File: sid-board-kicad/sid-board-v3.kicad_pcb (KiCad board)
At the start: 2 copper layers, 35.4 x 89.2 mm, 49 parts, among them J1 SPI + UART, J2 USB_B_Micro, J3 UART, Q1 BSS138, Q2 BSS138, SW1 SW_EN, SW2 SW_FLASH, U1 SC16IS752IPW, U2 MCP1703A-3302_SOT223, U3 SN65HVD232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

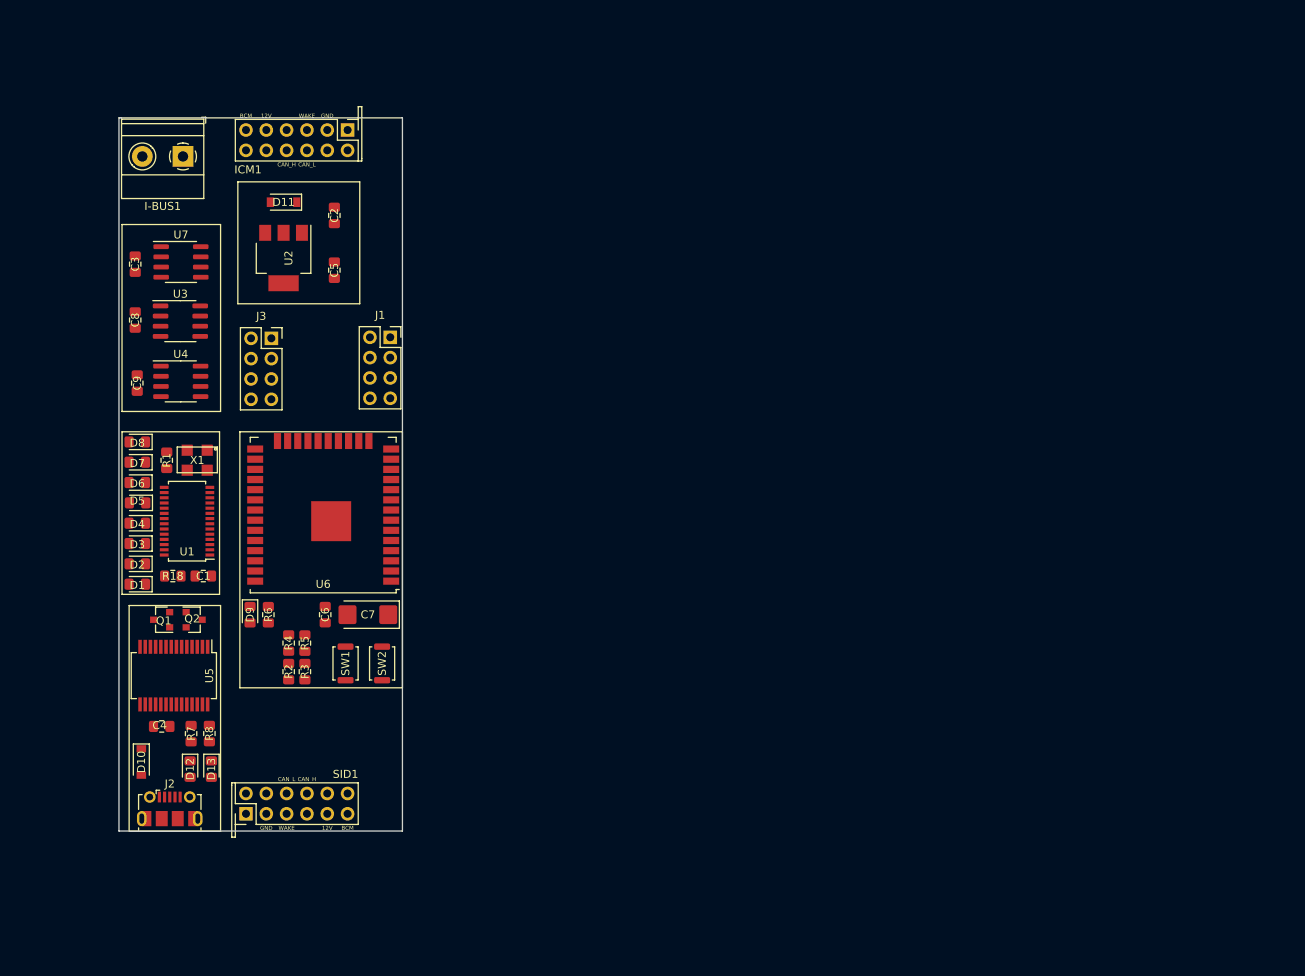
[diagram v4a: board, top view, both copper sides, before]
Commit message: Labelling and reorganisation
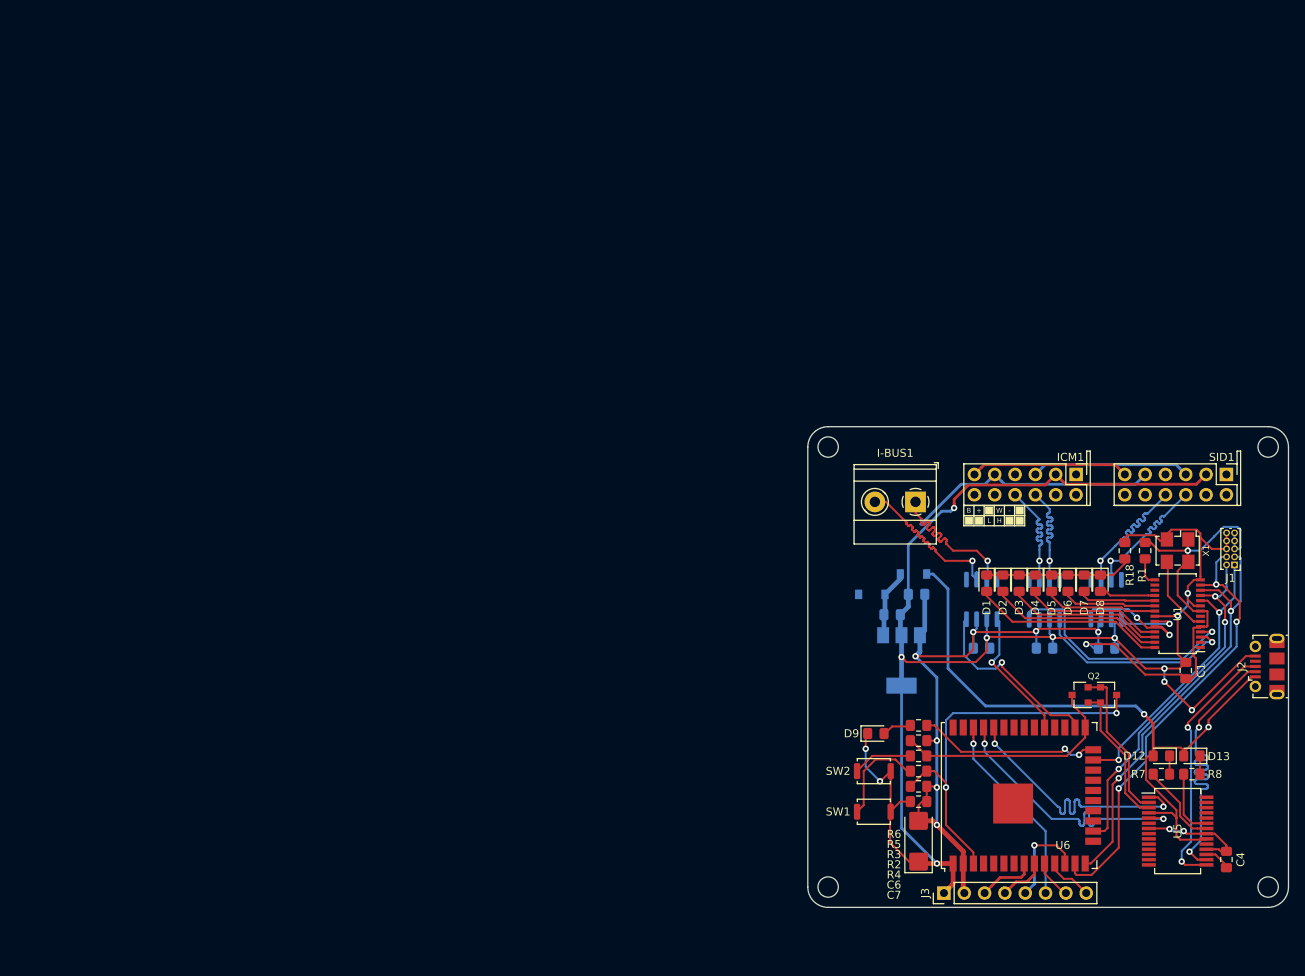
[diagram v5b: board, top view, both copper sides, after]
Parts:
- added ?: , , F.Cu at (123.2, 81.3)
- added ?: , , F.Cu at (121.9, 81.9)
- C2, C3, C5, C8, C9, D10, D11, U2, U3, U4, U7: moved to B.Cu
- J1: footprint Connector_PinSocket_2.54mm:PinSocket_2x04_P2.54mm_Vertical -> Connector_PinHeader_1.00mm:PinHeader_2x05_P1.00mm_Vertical
- J3: value UART -> Conn_01x08; footprint Connector_PinSocket_2.54mm:PinSocket_2x04_P2.54mm_Vertical -> Connector_PinHeader_2.54mm:PinHeader_1x08_P2.54mm_Vertical
- X1: value S53305-24.000-X -> ASE-xxxMHz; footprint sid-board:S53305-16.000-X -> Oscillator:Oscillator_SMD_EuroQuartz_XO53-4Pin_5.0x3.2mm_HandSoldering
- moved J2 138.3 mm to (170.2, 93.2), turned to 90 degrees
- moved C4 134.1 mm to (165.1, 117.3), turned to 90 degrees
- moved U5 127.0 mm to (159.0, 113.8), turned to 0 degrees
- moved C9 125.6 mm to (150.1, 90.9), turned to 0 degrees
- moved U1 124.4 mm to (159.0, 86.6)
- moved C1 123.4 mm to (160.0, 93.7), turned to 90 degrees
- moved X1 123.1 mm to (159.0, 78.7)
- moved R8 122.9 mm to (160.8, 106.7), turned to 0 degrees
- moved R1 122.8 mm to (154.9, 78.7)
- moved D13 122.6 mm to (160.8, 104.4), turned to 180 degrees
- moved D8 121.7 mm to (149.4, 82.8), turned to 270 degrees
- moved D12 121.4 mm to (157.0, 104.4), turned to 180 degrees
- moved R7 121.4 mm to (157.0, 106.7), turned to 0 degrees
- moved C8 120.8 mm to (142.4, 90.9), turned to 0 degrees
- moved D7 119.3 mm to (147.3, 82.8), turned to 270 degrees
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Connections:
- C2 pad 2: Net-(C2-Pad2) -> GND
- C5 pad 2: Net-(C2-Pad2) -> GND
- I-BUS1 pad 1: CAN_L -> CAN_H
- I-BUS1 pad 2: CAN_H -> CAN_L
- ICM1 pad 1: (no net) -> Net-(ICM1-Pad1)
- ICM1 pad 10: CAN_A_L -> CAN_A_H
- ICM1 pad 11: (no net) -> Net-(ICM1-Pad11)
- ICM1 pad 12: (no net) -> Net-(ICM1-Pad12)
- ICM1 pad 4: (no net) -> Net-(ICM1-Pad4)
- ICM1 pad 7: (no net) -> Net-(ICM1-Pad7)
- ICM1 pad 8: (no net) -> Net-(ICM1-Pad8)
- ICM1 pad 9: CAN_A_H -> CAN_A_L
- J1 pad 2: CLK -> MOSI
- J1 pad 3: MOSI -> MISO
- J1 pad 4: MISO -> CLK
- J1 pad 5: GND -> VDD_3.3V
- J1 pad 6: VDD_3.3V -> GND
- J1 pad 7: TXA -> VDD_3.3V
- J1 pad 8: RXA -> GND
- J2 pad 4: (no net) -> Net-(J2-Pad4)
- J3 pad 1: TX_ESP32 -> GND
- J3 pad 2: RX_ESP32 -> VDD_3.3V
- J3 pad 3: TX_ESP32_CAN -> Net-(J3-Pad3)
- J3 pad 4: RX_ESP32_CAN -> Net-(J3-Pad4)
- J3 pad 5: GND -> Net-(J3-Pad5)
- J3 pad 6: VDD_3.3V -> I2S_DIN
- J3 pad 7: TXB -> I2S_WSEL
- J3 pad 8: RXB -> I2S_BCLK
- SID1 pad 1: (no net) -> Net-(SID1-Pad1)
- SID1 pad 10: CAN_B_L -> CAN_B_H
- SID1 pad 11: (no net) -> Net-(SID1-Pad11)
- SID1 pad 12: (no net) -> Net-(SID1-Pad12)
- SID1 pad 4: (no net) -> Net-(SID1-Pad4)
- SID1 pad 7: (no net) -> Net-(SID1-Pad7)
- SID1 pad 8: (no net) -> Net-(SID1-Pad8)
- SID1 pad 9: CAN_B_H -> CAN_B_L
- U1 pad 1: (no net) -> Net-(U1-Pad1)
- U1 pad 16: (no net) -> Net-(U1-Pad16)
- U1 pad 17: (no net) -> Net-(U1-Pad17)
- U1 pad 2: (no net) -> Net-(U1-Pad2)
- U1 pad 7: (no net) -> Net-(U1-Pad7)
- U2 pad 2: Net-(C2-Pad2) -> GND
- U3 pad 5: (no net) -> Net-(U3-Pad5)
- U3 pad 8: (no net) -> Net-(U3-Pad8)
- U4 pad 5: (no net) -> Net-(U4-Pad5)
- U4 pad 8: (no net) -> Net-(U4-Pad8)
- U5 pad 10: (no net) -> Net-(U5-Pad10)
- U5 pad 11: (no net) -> Net-(U5-Pad11)
- U5 pad 12: SLEEP -> Net-(U5-Pad12)
- U5 pad 13: (no net) -> Net-(U5-Pad13)
- U5 pad 14: (no net) -> Net-(U5-Pad14)
- U5 pad 19: (no net) -> Net-(U5-Pad19)
- U5 pad 24: (no net) -> Net-(U5-Pad24)
- U5 pad 25: (no net) -> Net-(U5-Pad25)
- U5 pad 26: (no net) -> Net-(U5-Pad26)
- U5 pad 27: (no net) -> Net-(U5-Pad27)
- U5 pad 28: (no net) -> Net-(U5-Pad28)
- U5 pad 6: RI -> Net-(U5-Pad6)
- U5 pad 8: (no net) -> Net-(U5-Pad8)
- U5 pad 9: (no net) -> Net-(U5-Pad9)
- U6 pad 10: (no net) -> I2S_WSEL
- U6 pad 11: (no net) -> I2S_BCLK
- U6 pad 12: (no net) -> Net-(J3-Pad5)
- U6 pad 17: (no net) -> Net-(U6-Pad17)
- U6 pad 18: (no net) -> Net-(U6-Pad18)
- U6 pad 19: (no net) -> Net-(U6-Pad19)
- U6 pad 20: (no net) -> Net-(U6-Pad20)
- U6 pad 21: (no net) -> Net-(U6-Pad21)
- U6 pad 22: (no net) -> Net-(U6-Pad22)
- U6 pad 27: RI -> Net-(U6-Pad27)
- U6 pad 28: SLEEP -> Net-(U6-Pad28)
- U6 pad 30: (no net) -> Net-(U6-Pad30)
- U6 pad 31: (no net) -> Net-(U6-Pad31)
- U6 pad 32: (no net) -> Net-(U6-Pad32)
- U6 pad 33: (no net) -> Net-(U6-Pad33)
- U6 pad 36: (no net) -> I2S_DIN
- U6 pad 37: (no net) -> Net-(U6-Pad37)
- U6 pad 4: (no net) -> Net-(U6-Pad4)
- U6 pad 5: (no net) -> Net-(U6-Pad5)
- U6 pad 6: (no net) -> Net-(U6-Pad6)
- U6 pad 7: (no net) -> Net-(U6-Pad7)
- U6 pad 8: (no net) -> Net-(J3-Pad3)
- U6 pad 9: (no net) -> Net-(J3-Pad4)
- U7 pad 5: (no net) -> Net-(U7-Pad5)
- U7 pad 8: (no net) -> Net-(U7-Pad8)
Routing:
- net GND: track 0.00 -> 245.0 mm, vias 0 -> 15
- net VDD_3.3V: track 0.00 -> 151.7 mm, vias 0 -> 9
- net VBUS: track 0.00 -> 84.7 mm, vias 0 -> 2
- net CLK: track 0.00 -> 55.3 mm, vias 0 -> 3
- net MISO: track 0.00 -> 53.0 mm, vias 0 -> 2
- net EN: track 0.00 -> 49.7 mm, vias 0 -> 2
- net MOSI: track 0.00 -> 44.3 mm, vias 0 -> 3
- net USB_DM: track 0.00 -> 39.8 mm, vias 0 -> 2
- net CS: track 0.00 -> 36.5 mm, vias 0 -> 2
- net RX_ESP32: track 0.00 -> 35.4 mm, vias 0 -> 2
- net TX_ESP32: track 0.00 -> 35.0 mm, vias 0 -> 2
- net USB_DP: track 0.00 -> 32.6 mm, vias 0 -> 2
- net Net-(D11-Pad2): track 0.00 -> 31.6 mm
- net RXA: track 0.00 -> 31.1 mm, vias 0 -> 1
- net IO0: track 0.00 -> 29.6 mm
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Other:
- board size 35.4 x 89.2 mm -> 60.1 x 60.1 mm
- rule trace_min: 0.2 -> 0.1

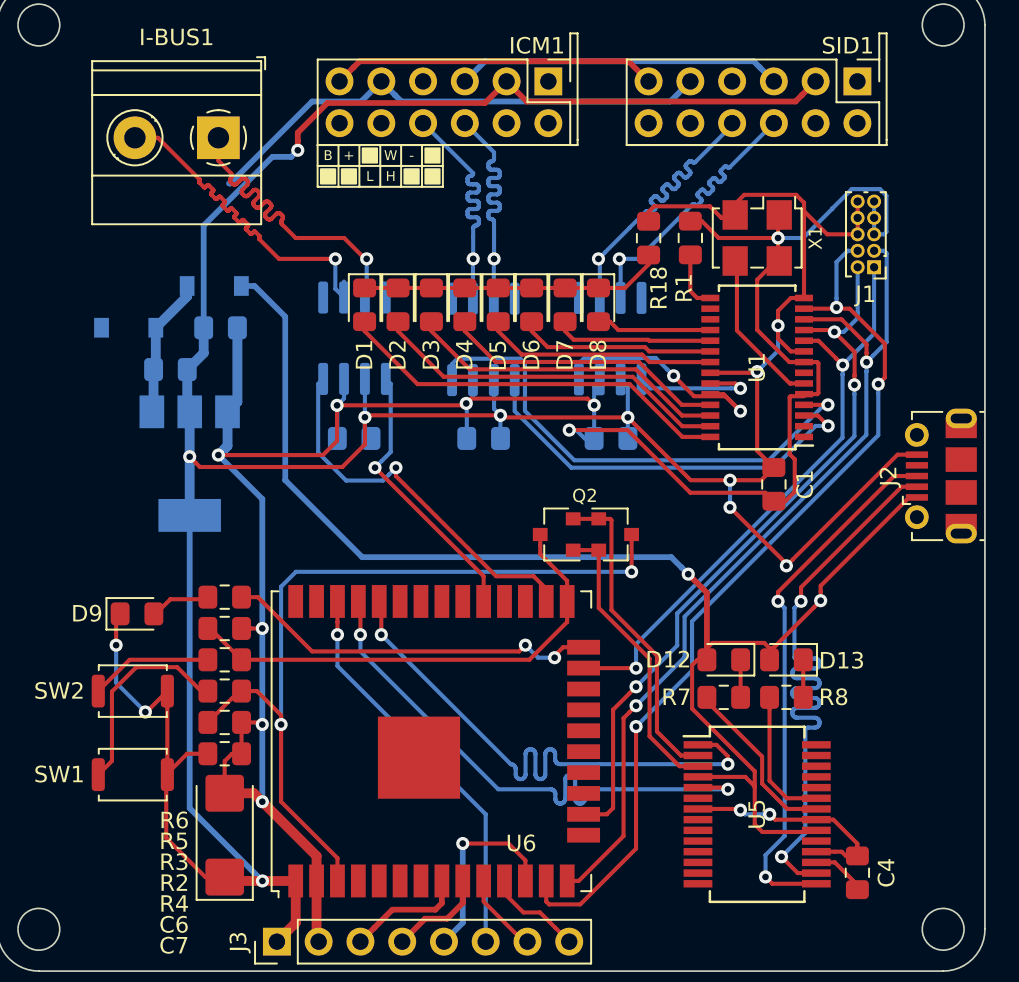
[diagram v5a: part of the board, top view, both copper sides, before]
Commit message: Lost labelling. Moved debug header.
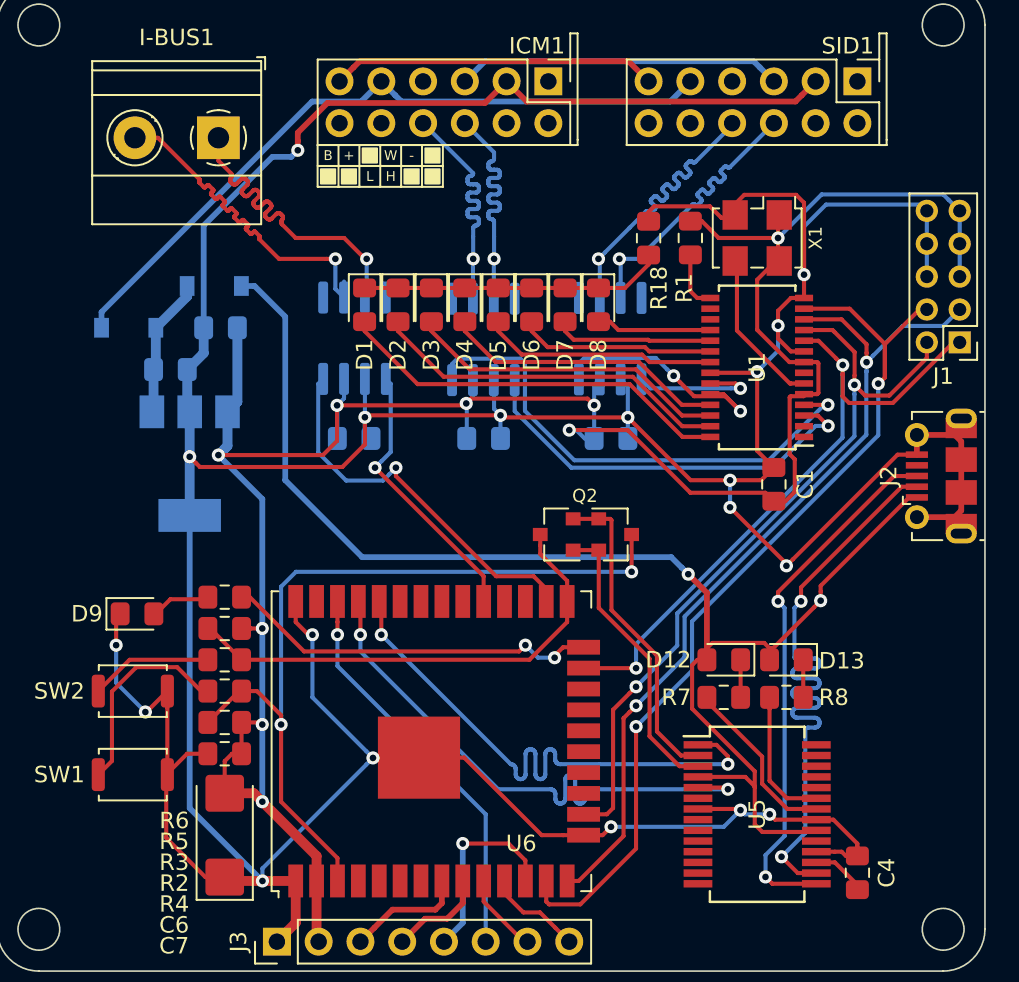
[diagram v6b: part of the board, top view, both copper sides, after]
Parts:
- removed ? (x2): , 
- J1: footprint Connector_PinHeader_1.00mm:PinHeader_2x05_P1.00mm_Vertical -> Connector_PinHeader_2.00mm:PinHeader_2x05_P2.00mm_Vertical
- moved J1 6.93 mm to (171.3, 85.1)
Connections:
- ICM1 pad 1: Net-(ICM1-Pad1) -> (no net)
- ICM1 pad 11: Net-(ICM1-Pad11) -> (no net)
- ICM1 pad 12: Net-(ICM1-Pad12) -> (no net)
- ICM1 pad 4: Net-(ICM1-Pad4) -> (no net)
- ICM1 pad 7: Net-(ICM1-Pad7) -> (no net)
- ICM1 pad 8: Net-(ICM1-Pad8) -> (no net)
- J2 pad 4: Net-(J2-Pad4) -> (no net)
- SID1 pad 1: Net-(SID1-Pad1) -> (no net)
- SID1 pad 11: Net-(SID1-Pad11) -> (no net)
- SID1 pad 12: Net-(SID1-Pad12) -> (no net)
- SID1 pad 4: Net-(SID1-Pad4) -> (no net)
- SID1 pad 7: Net-(SID1-Pad7) -> (no net)
- SID1 pad 8: Net-(SID1-Pad8) -> (no net)
- U1 pad 1: Net-(U1-Pad1) -> (no net)
- U1 pad 16: Net-(U1-Pad16) -> (no net)
- U1 pad 17: Net-(U1-Pad17) -> (no net)
- U1 pad 2: Net-(U1-Pad2) -> (no net)
- U1 pad 7: Net-(U1-Pad7) -> (no net)
- U3 pad 5: Net-(U3-Pad5) -> (no net)
- U3 pad 8: Net-(U3-Pad8) -> (no net)
- U4 pad 5: Net-(U4-Pad5) -> (no net)
- U4 pad 8: Net-(U4-Pad8) -> (no net)
- U5 pad 10: Net-(U5-Pad10) -> (no net)
- U5 pad 11: Net-(U5-Pad11) -> (no net)
- U5 pad 12: Net-(U5-Pad12) -> (no net)
- U5 pad 13: Net-(U5-Pad13) -> (no net)
- U5 pad 14: Net-(U5-Pad14) -> (no net)
- U5 pad 19: Net-(U5-Pad19) -> (no net)
- U5 pad 24: Net-(U5-Pad24) -> (no net)
- U5 pad 25: Net-(U5-Pad25) -> (no net)
- U5 pad 26: Net-(U5-Pad26) -> (no net)
- U5 pad 27: Net-(U5-Pad27) -> (no net)
- U5 pad 28: Net-(U5-Pad28) -> (no net)
- U5 pad 6: Net-(U5-Pad6) -> (no net)
- U5 pad 8: Net-(U5-Pad8) -> (no net)
- U5 pad 9: Net-(U5-Pad9) -> (no net)
- U6 pad 17: Net-(U6-Pad17) -> (no net)
- U6 pad 18: Net-(U6-Pad18) -> (no net)
- U6 pad 19: Net-(U6-Pad19) -> (no net)
- U6 pad 20: Net-(U6-Pad20) -> (no net)
- U6 pad 21: Net-(U6-Pad21) -> (no net)
- U6 pad 22: Net-(U6-Pad22) -> (no net)
- U6 pad 27: Net-(U6-Pad27) -> (no net)
- U6 pad 28: Net-(U6-Pad28) -> (no net)
- U6 pad 30: Net-(U6-Pad30) -> (no net)
- U6 pad 31: Net-(U6-Pad31) -> (no net)
- U6 pad 32: Net-(U6-Pad32) -> (no net)
- U6 pad 33: Net-(U6-Pad33) -> (no net)
- U6 pad 37: Net-(U6-Pad37) -> (no net)
- U6 pad 4: Net-(U6-Pad4) -> (no net)
- U6 pad 5: Net-(U6-Pad5) -> (no net)
- U6 pad 6: Net-(U6-Pad6) -> (no net)
- U6 pad 7: Net-(U6-Pad7) -> (no net)
- U7 pad 5: Net-(U7-Pad5) -> (no net)
- U7 pad 8: Net-(U7-Pad8) -> (no net)
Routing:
- net GND: track 245.0 -> 312.2 mm, vias 15 -> 19
- net Net-(D11-Pad2): track 31.6 -> 43.6 mm
- net CS: track 36.5 -> 40.5 mm
- net VDD_3.3V: track 151.7 -> 155.2 mm
- net MOSI: track 44.3 -> 46.0 mm, vias 3 -> 2
- net CLK: track 55.3 -> 56.4 mm, vias 3 -> 2
- net MISO: track 53.0 -> 52.0 mm

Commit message: Re-labelling everything
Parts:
- BSS138: renamed from Q2; value BSS138 -> BSS138 x2
- D12: value LED0 -> LED9
- D13: value LED0 -> LED8
- D9: value LED_IO2 -> LED_10
- J2: value USB_B_Micro -> ESP32 UART
- SW1: value SW_EN -> EN
- SW2: value SW_FLASH -> FLASH
- U1: value SC16IS752IPW -> SC16IS752
- U2: value MCP1703A-3302_SOT223 -> MCP1703A-3302
- U3: value SN65HVD232 -> SN65HVD232 x3
- U5: value CY7C65213-28PVXI -> CY7C65213
- X1: value ASE-xxxMHz -> 24MHz
- moved D9 3.43 mm to (117.9, 101.6)
- moved SW1 3.18 mm to (117.9, 111.4)
- moved SW2 3.18 mm to (117.9, 106.3)
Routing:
- net Net-(R3-Pad2): track 7.45 -> 11.7 mm
- net Net-(D9-Pad2): track 3.70 -> 7.54 mm
- net GND: track 312.2 -> 314.8 mm
- net Net-(R2-Pad2): track 12.4 -> 11.9 mm
